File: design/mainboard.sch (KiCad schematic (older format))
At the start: 0 parts

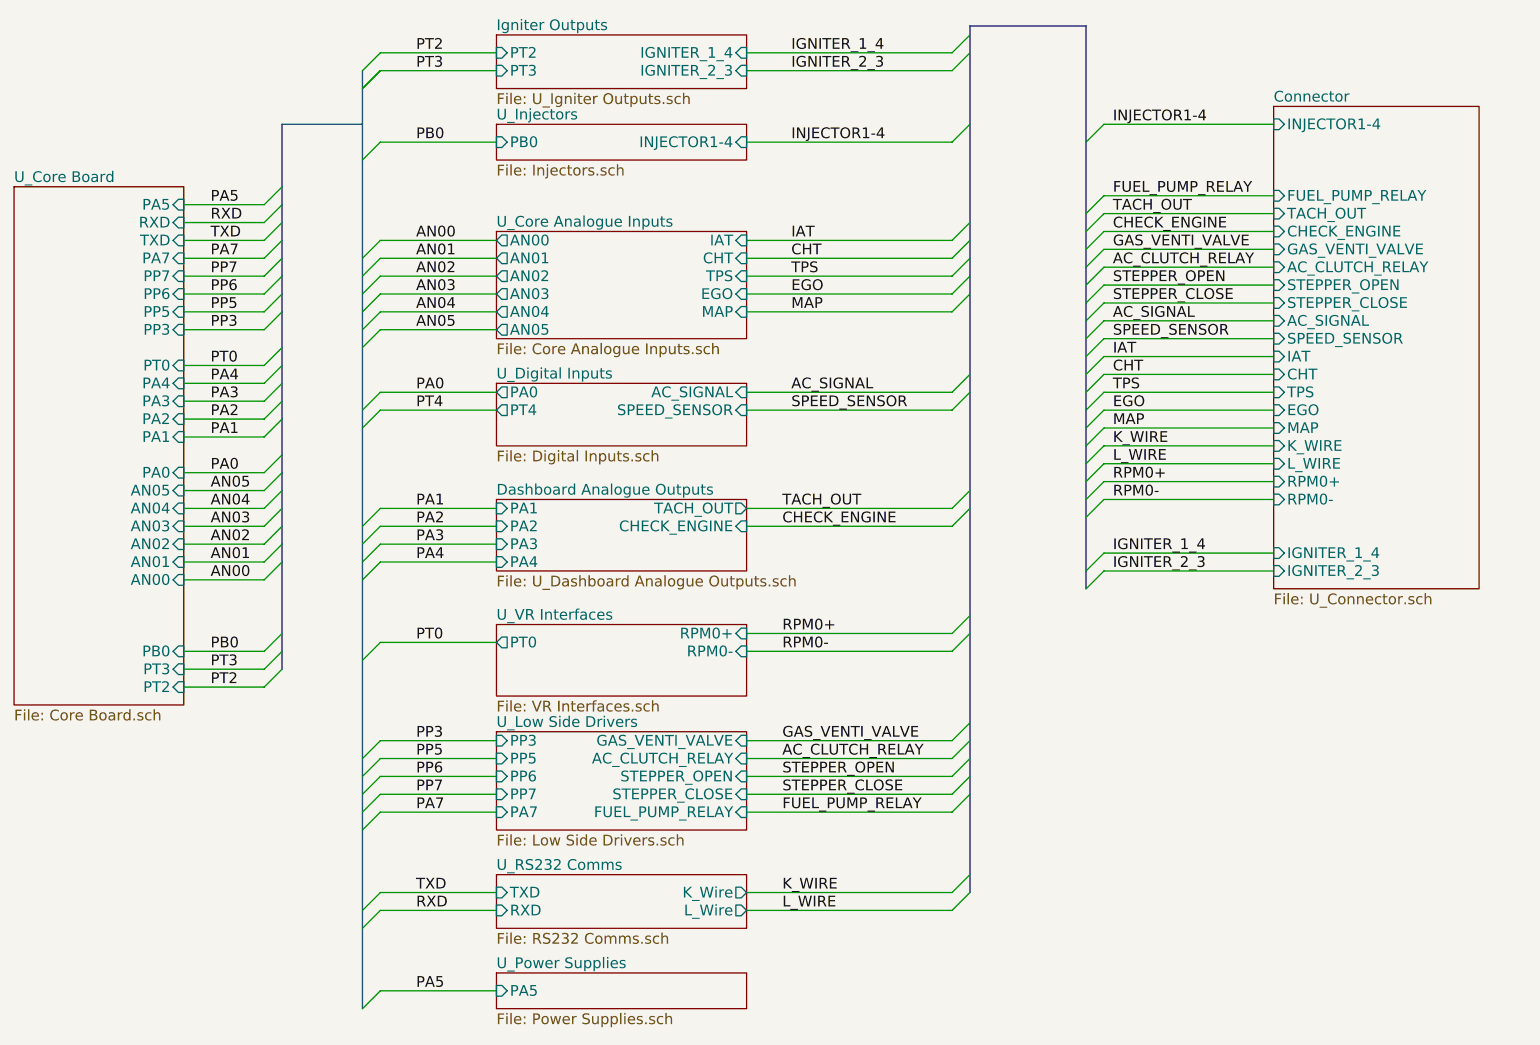
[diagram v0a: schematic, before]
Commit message: revise schema to be full pin compatible with stock ECU
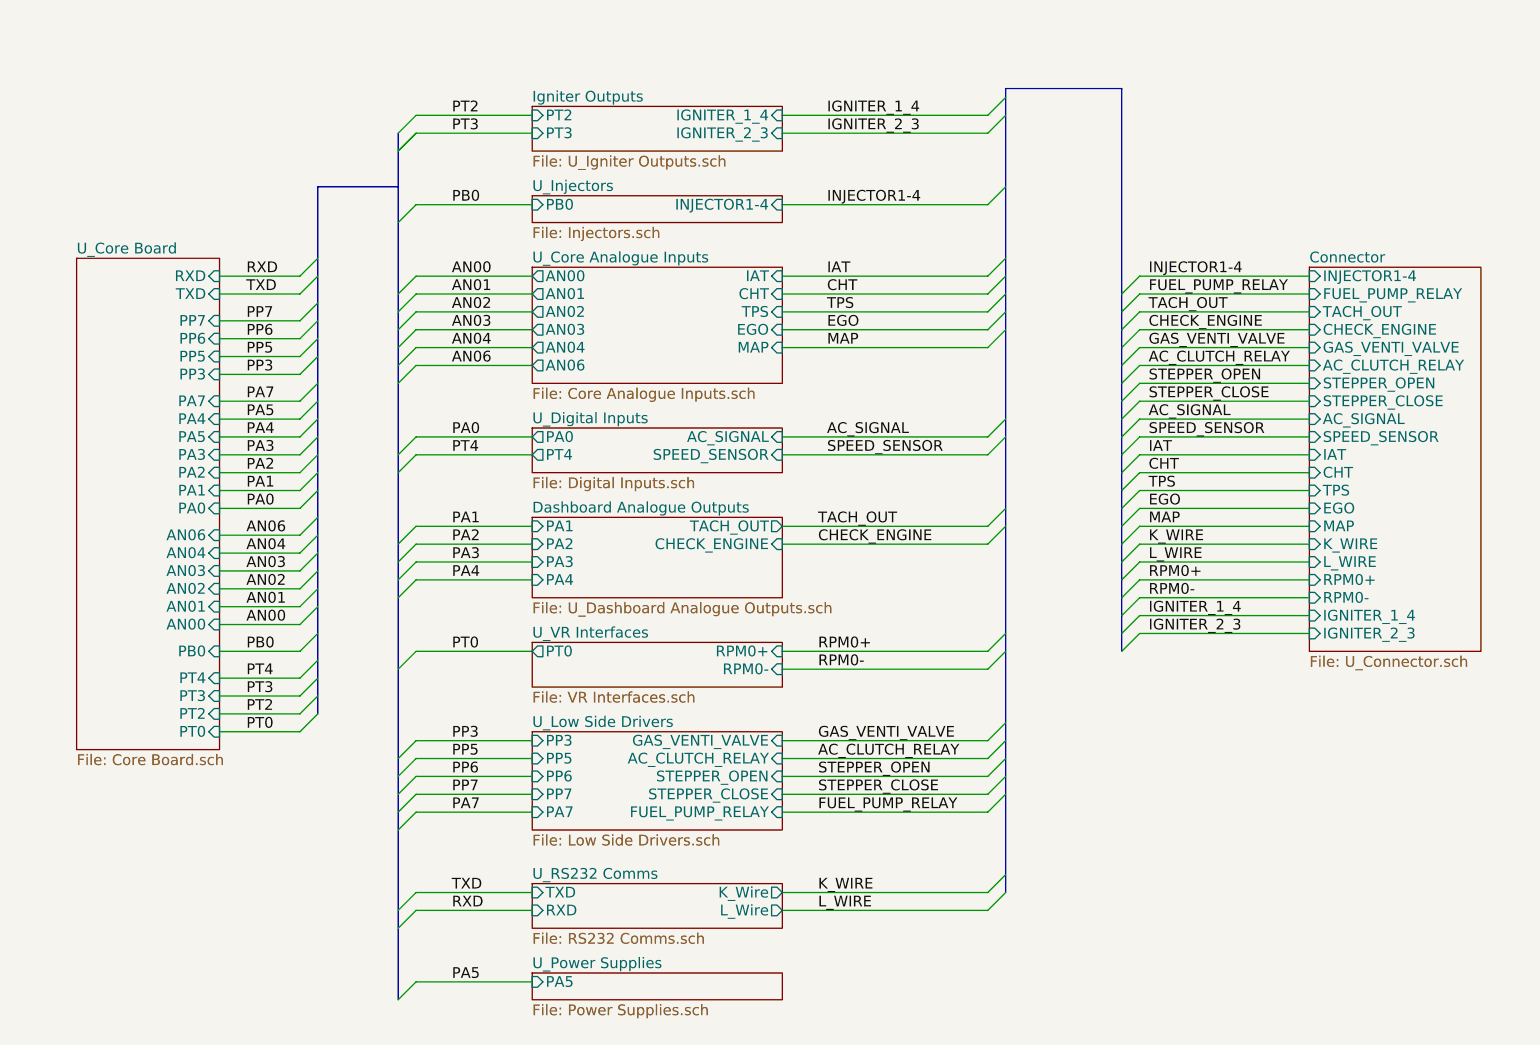
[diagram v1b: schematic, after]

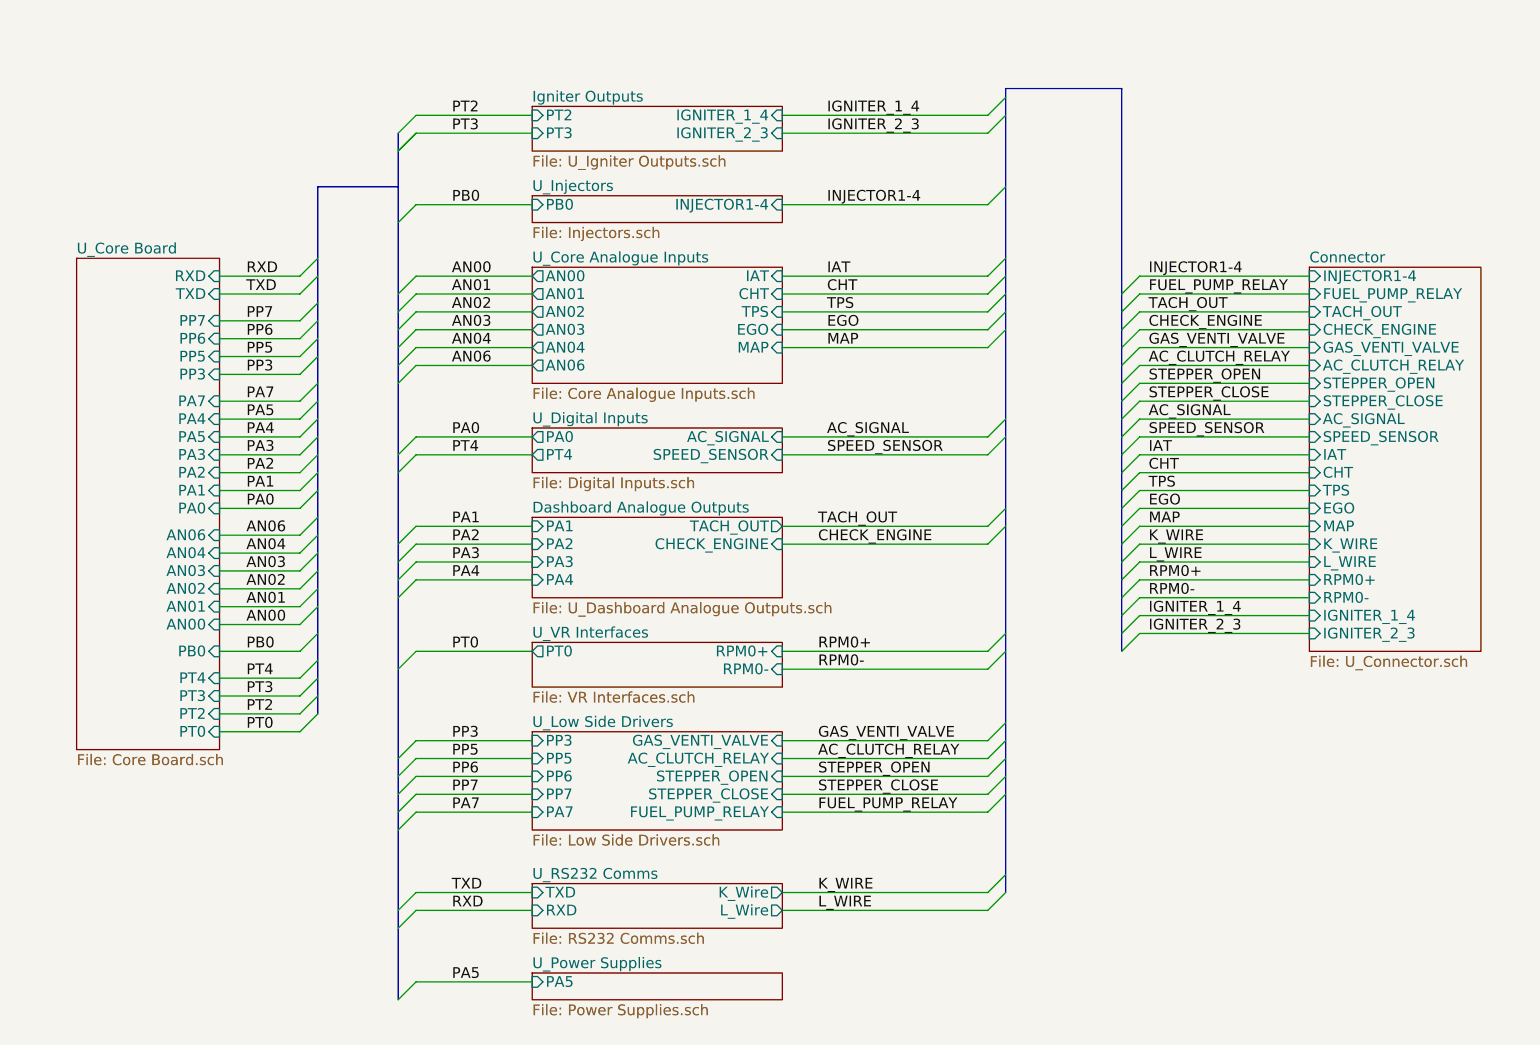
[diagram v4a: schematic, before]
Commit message: use max9924 to replace ncv1124, add narrow band oxygen sensor differential input circuit, put all component into PCB edge
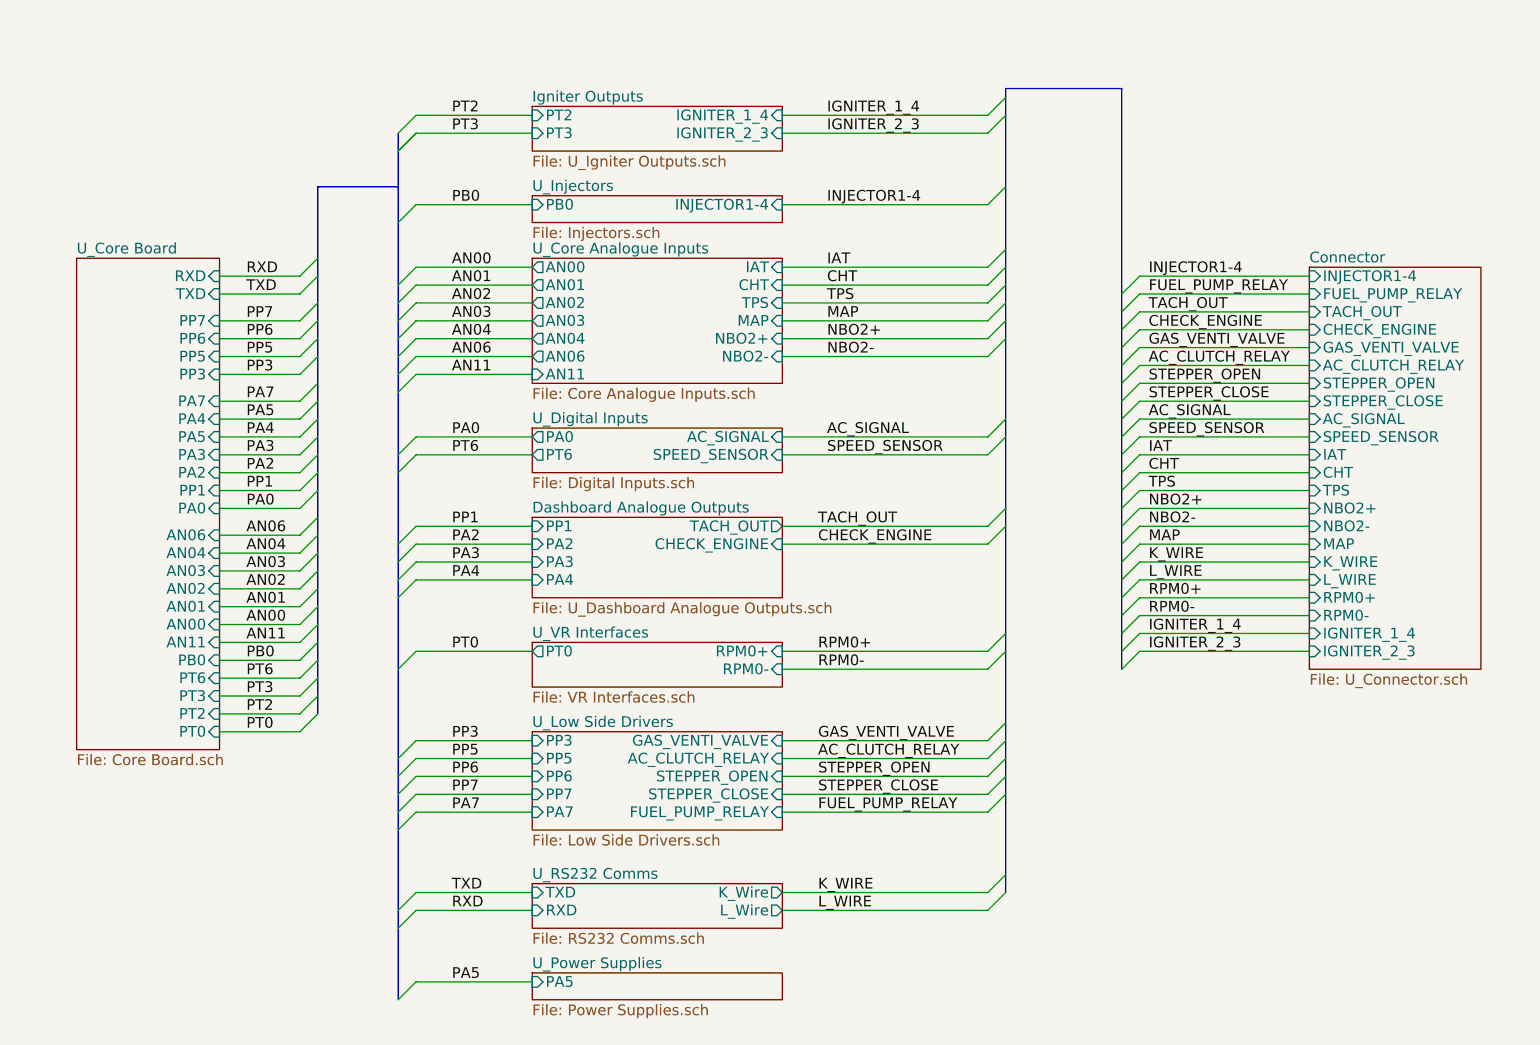
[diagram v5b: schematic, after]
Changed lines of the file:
@@
-EESchema Schematic File Version 2  date 14/01/2012 13:46:11
+EESchema Schematic File Version 2  date 21/01/2012 01:12:26
 LIBS:power
 LIBS:device
@@
 LIBS:contrib
 LIBS:valves
+LIBS:freeEMS_lib
 LIBS:mainboard-cache
 EELAYER 25  0
@@
 Sheet 1 12
 Title "CatSquirt main board(code migrant worker)"
-Date "14 jan 2012"
+Date "20 jan 2012"
 Rev "0.01"
 Comp "diyefi.org"
@@
 Comment4 ""
 $EndDescr
-$Sheet
-S 4350 2400 1400 650
-U 4E918900
-F0 "U_Core Analogue Inputs" 60
-F1 "Core Analogue Inputs.sch" 60
-F2 "MAP" I R 5750 2850 60
-F3 "AN04" O L 4350 2850 60
-F4 "TPS" I R 5750 2650 60
-F5 "AN02" O L 4350 2650 60
-F6 "AN01" O L 4350 2550 60
-F7 "CHT" I R 5750 2550 60
-F8 "AN03" O L 4350 2750 60
-F9 "EGO" I R 5750 2750 60
-F10 "IAT" I R 5750 2450 60
-F11 "AN00" O L 4350 2450 60
-F12 "AN06" O L 4350 2950 60
-$EndSheet
+Text Label 2750 4500 0    60   ~ 0
+AN11
+Entry Wire Line
+	3050 4500 3150 4400
+Wire Wire Line
+	2600 4500 3050 4500
+Wire Wire Line
+	5750 2900 6900 2900
+Wire Wire Line
+	7750 4550 8700 4550
 Wire Wire Line
 	3700 6400 4350 6400
@@
 	4350 3450 3700 3450
 Wire Wire Line
-	4350 2950 3700 2950
-Wire Wire Line
-	4350 2750 3700 2750
-Wire Wire Line
-	4350 2550 3700 2550
+	4350 2900 3700 2900
+Wire Wire Line
+	4350 2700 3700 2700
+Wire Wire Line
+	4350 2500 3700 2500
 Wire Wire Line
 	4350 1650 3700 1650
@@
 	5750 3450 6900 3450
 Wire Wire Line
-	5750 2850 6900 2850
-Wire Wire Line
-	5750 2650 6900 2650
-Wire Wire Line
-	5750 2450 6900 2450
+	5750 2800 6900 2800
+Wire Wire Line
+	5750 2600 6900 2600
+Wire Wire Line
+	5750 2400 6900 2400
 Wire Wire Line
 	5750 1550 6900 1550
@@
 Wire Bus Line
 	7000 1400 7650 1400
-Wire Bus Line
-	7650 1400 7650 4550
 Wire Wire Line
 	5750 1650 6900 1650
 Wire Wire Line
-	5750 2550 6900 2550
-Wire Wire Line
-	6900 2750 5750 2750
+	5750 2500 6900 2500
+Wire Wire Line
+	6900 2700 5750 2700
 Wire Wire Line
 	5750 3350 6900 3350
@@
 	4350 1550 3700 1550
 Wire Wire Line
-	4350 2450 3700 2450
-Wire Wire Line
-	4350 2650 3700 2650
-Wire Wire Line
-	4350 2850 3700 2850
+	4350 2400 3700 2400
+Wire Wire Line
+	4350 2600 3700 2600
+Wire Wire Line
+	4350 2800 3700 2800
 Wire Wire Line
 	4350 3350 3700 3350
@@
 	2600 4300 3050 4300
 Wire Wire Line
-	2600 4550 3050 4550
-Wire Wire Line
 	2600 4800 3050 4800
 Wire Wire Line
@@
 Wire Wire Line
 	8700 2550 7750 2550
+Wire Bus Line
+	7650 1400 7650 4650
+Wire Wire Line
+	4350 3000 3700 3000
+Wire Wire Line
+	2600 4600 3050 4600
+Text Label 6000 2900 0    60   ~ 0
+NBO2-
+Entry Wire Line
+	6900 2900 7000 2800
+Text Label 3900 3000 0    60   ~ 0
+AN11
+Entry Wire Line
+	3600 3100 3700 3000
+Text Label 7800 3850 0    60   ~ 0
+NBO2-
+Entry Wire Line
+	7650 4650 7750 4550
+$Sheet
+S 4350 3300 1400 250
+U 4E939A82
+F0 "U_Digital Inputs" 60
+F1 "Digital Inputs.sch" 60
+F2 "AC_SIGNAL" I R 5750 3350 60
+F3 "PA0" O L 4350 3350 60
+F4 "SPEED_SENSOR" I R 5750 3450 60
+F5 "PT6" O L 4350 3450 60
+$EndSheet
+$Sheet
+S 4350 3800 1400 450
+U 4E939ACE
+F0 "Dashboard Analogue Outputs" 60
+F1 "U_Dashboard Analogue Outputs.sch" 60
+F2 "PA2" I L 4350 3950 60
+F3 "PA3" I L 4350 4050 60
+F4 "TACH_OUT" O R 5750 3850 60
+F5 "CHECK_ENGINE" I R 5750 3950 60
+F6 "PA4" I L 4350 4150 60
+F7 "PP1" I L 4350 3850 60
+$EndSheet
+$Sheet
+S 4350 2350 1400 700
+U 4E918900
+F0 "U_Core Analogue Inputs" 60
+F1 "Core Analogue Inputs.sch" 60
+F2 "MAP" I R 5750 2700 60
+F3 "AN04" O L 4350 2800 60
+F4 "TPS" I R 5750 2600 60
+F5 "AN02" O L 4350 2600 60
+F6 "AN01" O L 4350 2500 60
+F7 "CHT" I R 5750 2500 60
+F8 "AN03" O L 4350 2700 60
+F9 "IAT" I R 5750 2400 60
+F10 "AN00" O L 4350 2400 60
+F11 "AN06" O L 4350 2900 60
+F12 "AN11" I L 4350 3000 60
+F13 "NBO2-" I R 5750 2900 60
+F14 "NBO2+" I R 5750 2800 60
+$EndSheet
 Entry Wire Line
 	3050 5000 3150 4900
 Text Label 2750 4700 0    60   ~ 0
-PT4
+PT6
 Entry Wire Line
 	3050 4700 3150 4600
@@
 F12 "PA3" I R 2600 3450 60
 F13 "PA2" I R 2600 3550 60
-F14 "PA1" I R 2600 3650 60
-F15 "PA0" I R 2600 3750 60
-F16 "AN04" I R 2600 4000 60
-F17 "AN03" I R 2600 4100 60
-F18 "AN02" I R 2600 4200 60
-F19 "AN01" I R 2600 4300 60
-F20 "AN00" I R 2600 4400 60
-F21 "PB0" I R 2600 4550 60
-F22 "PT3" I R 2600 4800 60
-F23 "PT2" I R 2600 4900 60
-F24 "PT4" I R 2600 4700 60
-F25 "AN06" I R 2600 3900 60
+F14 "PA0" I R 2600 3750 60
+F15 "AN04" I R 2600 4000 60
+F16 "AN03" I R 2600 4100 60
+F17 "AN02" I R 2600 4200 60
+F18 "AN01" I R 2600 4300 60
+F19 "AN00" I R 2600 4400 60
+F20 "PB0" I R 2600 4600 60
+F21 "PT3" I R 2600 4800 60
+F22 "PT2" I R 2600 4900 60
+F23 "AN06" I R 2600 3900 60
+F24 "PT6" I R 2600 4700 60
+F25 "PP1" I R 2600 3650 60
+F26 "AN11" I R 2600 4500 60
 $EndSheet
 $Sheet
-S 8700 2400 960  2150
+S 8700 2400 960  2250
 U 4E951714
 F0 "Connector" 60
@@
 F5 "AC_CLUTCH_RELAY" I L 8700 2950 60
 F6 "GAS_VENTI_VALVE" I L 8700 2850 60
-F7 "RPM0-" I L 8700 4250 60
-F8 "RPM0+" I L 8700 4150 60
+F7 "RPM0-" I L 8700 4350 60
+F8 "RPM0+" I L 8700 4250 60
 F9 "CHECK_ENGINE" I L 8700 2750 60
 F10 "TACH_OUT" I L 8700 2650 60
 F11 "AC_SIGNAL" I L 8700 3250 60
-F12 "MAP" I L 8700 3850 60
-F13 "EGO" I L 8700 3750 60
-F14 "TPS" I L 8700 3650 60
-F15 "CHT" I L 8700 3550 60
-F16 "IAT" I L 8700 3450 60
-F17 "INJECTOR1-4" I L 8700 2450 60
-F18 "IGNITER_2_3" I L 8700 4450 60
-F19 "IGNITER_1_4" I L 8700 4350 60
-F20 "L_WIRE" I L 8700 4050 60
-F21 "K_WIRE" I L 8700 3950 60
-F22 "SPEED_SENSOR" I L 8700 3350 60
+F12 "MAP" I L 8700 3950 60
+F13 "TPS" I L 8700 3650 60
+F14 "CHT" I L 8700 3550 60
+F15 "IAT" I L 8700 3450 60
+F16 "INJECTOR1-4" I L 8700 2450 60
+F17 "IGNITER_2_3" I L 8700 4550 60
+F18 "IGNITER_1_4" I L 8700 4450 60
+F19 "L_WIRE" I L 8700 4150 60
+F20 "K_WIRE" I L 8700 4050 60
+F21 "SPEED_SENSOR" I L 8700 3350 60
+F22 "NBO2-" I L 8700 3850 60
+F23 "NBO2+" I L 8700 3750 60
 $EndSheet
 Text Label 2750 4900 0    60   ~ 0
@@
 Text Label 2750 4800 0    60   ~ 0
 PT3
-Text Label 2750 4550 0    60   ~ 0
+Text Label 2750 4600 0    60   ~ 0
 PB0
 Text Label 2750 4400 0    60   ~ 0
@@
 PA0
 Text Label 2750 3650 0    60   ~ 0
-PA1
+PP1
 Text Label 2750 3550 0    60   ~ 0
 PA2
@@
 	3050 4400 3150 4300
 Entry Wire Line
-	3050 4550 3150 4450
+	3050 4600 3150 4500
 Entry Wire Line
 	3050 4800 3150 4700
@@
 	3600 3450 3700 3350
 Entry Wire Line
-	3600 3050 3700 2950
-Entry Wire Line
-	3600 2950 3700 2850
-Entry Wire Line
-	3600 2850 3700 2750
-Entry Wire Line
-	3600 2750 3700 2650
-Entry Wire Line
-	3600 2650 3700 2550
-Entry Wire Line
-	3600 2550 3700 2450
+	3600 3000 3700 2900
+Entry Wire Line
+	3600 2900 3700 2800
+Entry Wire Line
+	3600 2800 3700 2700
+Entry Wire Line
+	3600 2700 3700 2600
+Entry Wire Line
+	3600 2600 3700 2500
+Entry Wire Line
+	3600 2500 3700 2400
 Entry Wire Line
 	3600 2150 3700 2050
@@
 PA2
 Text Label 3900 3850 0    60   ~ 0
-PA1
+PP1
 Text Label 3900 3450 0    60   ~ 0
-PT4
+PT6
 Text Label 3900 3350 0    60   ~ 0
 PA0
-Text Label 3900 2950 0    60   ~ 0
+Text Label 3900 2900 0    60   ~ 0
 AN06
-Text Label 3900 2850 0    60   ~ 0
+Text Label 3900 2800 0    60   ~ 0
 AN04
-Text Label 3900 2750 0    60   ~ 0
+Text Label 3900 2700 0    60   ~ 0
 AN03
-Text Label 3900 2650 0    60   ~ 0
+Text Label 3900 2600 0    60   ~ 0
 AN02
-Text Label 3900 2550 0    60   ~ 0
+Text Label 3900 2500 0    60   ~ 0
 AN01
-Text Label 3900 2450 0    60   ~ 0
+Text Label 3900 2400 0    60   ~ 0
 AN00
 Text Label 3900 2050 0    60   ~ 0
@@
 Text Label 3900 1550 0    60   ~ 0
 PT2
+Text Label 7800 4550 0    60   ~ 0
+IGNITER_2_3
 Text Label 7800 4450 0    60   ~ 0
-IGNITER_2_3
+IGNITER_1_4
 Text Label 7800 4350 0    60   ~ 0
-IGNITER_1_4
+RPM0-
 Text Label 7800 4250 0    60   ~ 0
-RPM0-
+RPM0+
 Text Label 7800 4150 0    60   ~ 0
-RPM0+
+L_WIRE
 Text Label 7800 4050 0    60   ~ 0
-L_WIRE
+K_WIRE
 Text Label 7800 3950 0    60   ~ 0
-K_WIRE
-Text Label 7800 3850 0    60   ~ 0
 MAP
 Text Label 7800 3750 0    60   ~ 0
-EGO
+NBO2+
 Text Label 7800 3650 0    60   ~ 0
 TPS
@@
 Text Label 5950 5900 0    60   ~ 0
 K_WIRE
-$Sheet
-S 4350 3800 1400 450
-U 4E939ACE
-F0 "Dashboard Analogue Outputs" 60
-F1 "U_Dashboard Analogue Outputs.sch" 60
-F2 "PA4" I L 4350 4150 60
-F3 "PA2" I L 4350 3950 60
-F4 "PA1" I L 4350 3850 60
-F5 "PA3" I L 4350 4050 60
-F6 "TACH_OUT" O R 5750 3850 60
-F7 "CHECK_ENGINE" I R 5750 3950 60
-$EndSheet
 Text Label 5950 4650 0    60   ~ 0
 RPM0-
@@
 Text Label 6000 3350 0    60   ~ 0
 AC_SIGNAL
-Text Label 6000 2850 0    60   ~ 0
+Text Label 6000 2700 0    60   ~ 0
 MAP
-Text Label 6000 2750 0    60   ~ 0
-EGO
-Text Label 6000 2650 0    60   ~ 0
+Text Label 6000 2800 0    60   ~ 0
+NBO2+
+Text Label 6000 2600 0    60   ~ 0
 TPS
-Text Label 6000 2550 0    60   ~ 0
+Text Label 6000 2500 0    60   ~ 0
 CHT
-Text Label 6000 2450 0    60   ~ 0
+Text Label 6000 2400 0    60   ~ 0
 IAT
 Text Label 6000 2050 0    60   ~ 0
@@
 IGNITER_2_3
 Entry Wire Line
-	6900 2750 7000 2650
+	6900 2700 7000 2600
 Entry Wire Line
 	6900 6000 7000 5900
@@
 	6900 2050 7000 1950
 Entry Wire Line
-	6900 2450 7000 2350
-Entry Wire Line
-	6900 2550 7000 2450
-Entry Wire Line
-	6900 2650 7000 2550
-Entry Wire Line
-	6900 2850 7000 2750
+	6900 2400 7000 2300
+Entry Wire Line
+	6900 2500 7000 2400
+Entry Wire Line
+	6900 2600 7000 2500
+Entry Wire Line
+	6900 2800 7000 2700
 Entry Wire Line
 	6900 3450 7000 3350
@@
 $EndSheet
 $Sheet
-S 4350 3300 1400 250
-U 4E939A82
-F0 "U_Digital Inputs" 60
-F1 "Digital Inputs.sch" 60
-F2 "AC_SIGNAL" I R 5750 3350 60
-F3 "PA0" O L 4350 3350 60
-F4 "PT4" O L 4350 3450 60
-F5 "SPEED_SENSOR" I R 5750 3450 60
-$EndSheet
-$Sheet
